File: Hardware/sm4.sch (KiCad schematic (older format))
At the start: 91 parts, among them J1 Motor1, J2 Termination, J3 CAN bus, J4 Motor2, J5 I2C, J6 Power, J7 USB_C_Receptacle_USB2.0, J8 Conn_01x05_Male, Q1 NDT2955, SW1 RST_SW, SW2 BOOT_SW, U1 STM32F412RETx, U2 TMC2100-TA, U3 MCP2562-E-SN, U4 TMC2100-TA, U6 MCP1700-3302E_SOT23, U7 USBLC6-2SC6, Y1 25 MHz

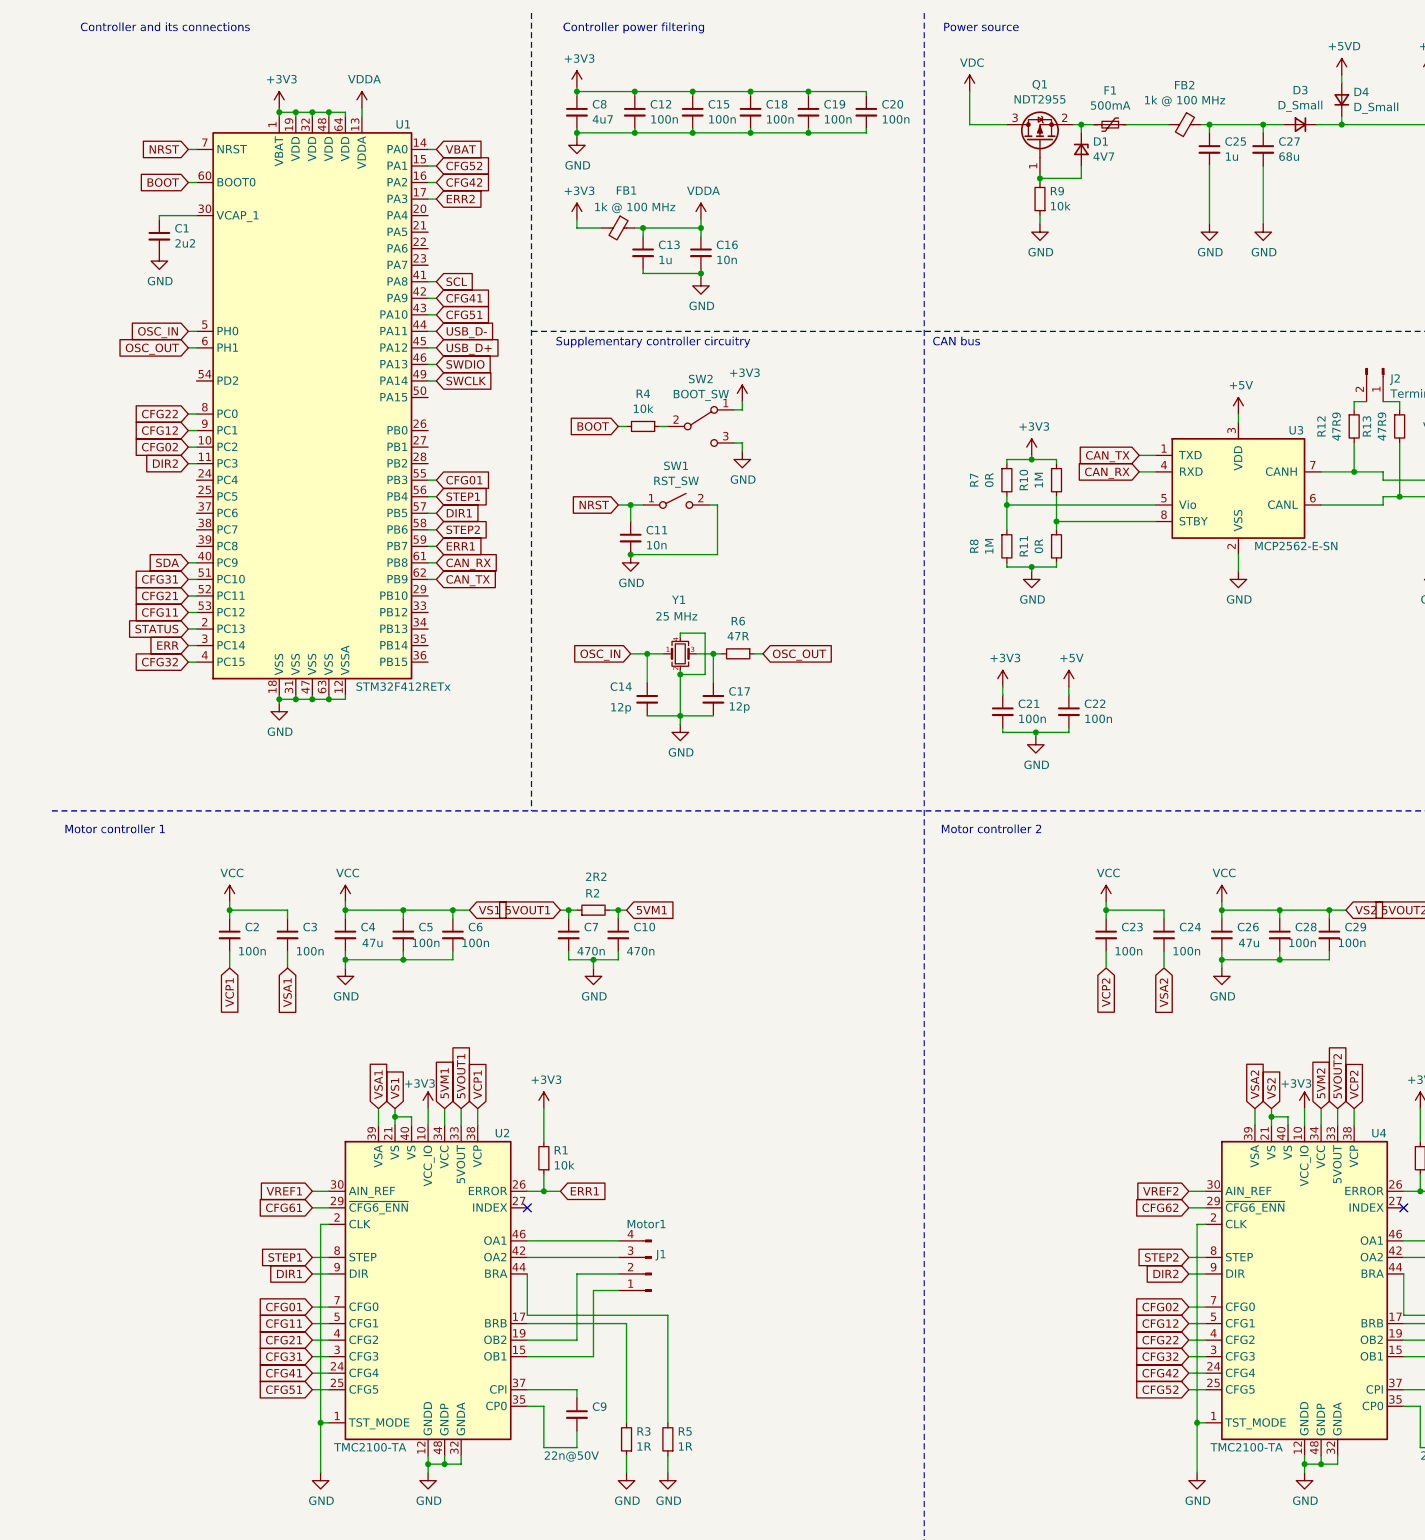
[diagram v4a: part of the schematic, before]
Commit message: Implement more of the second version of the PCB.
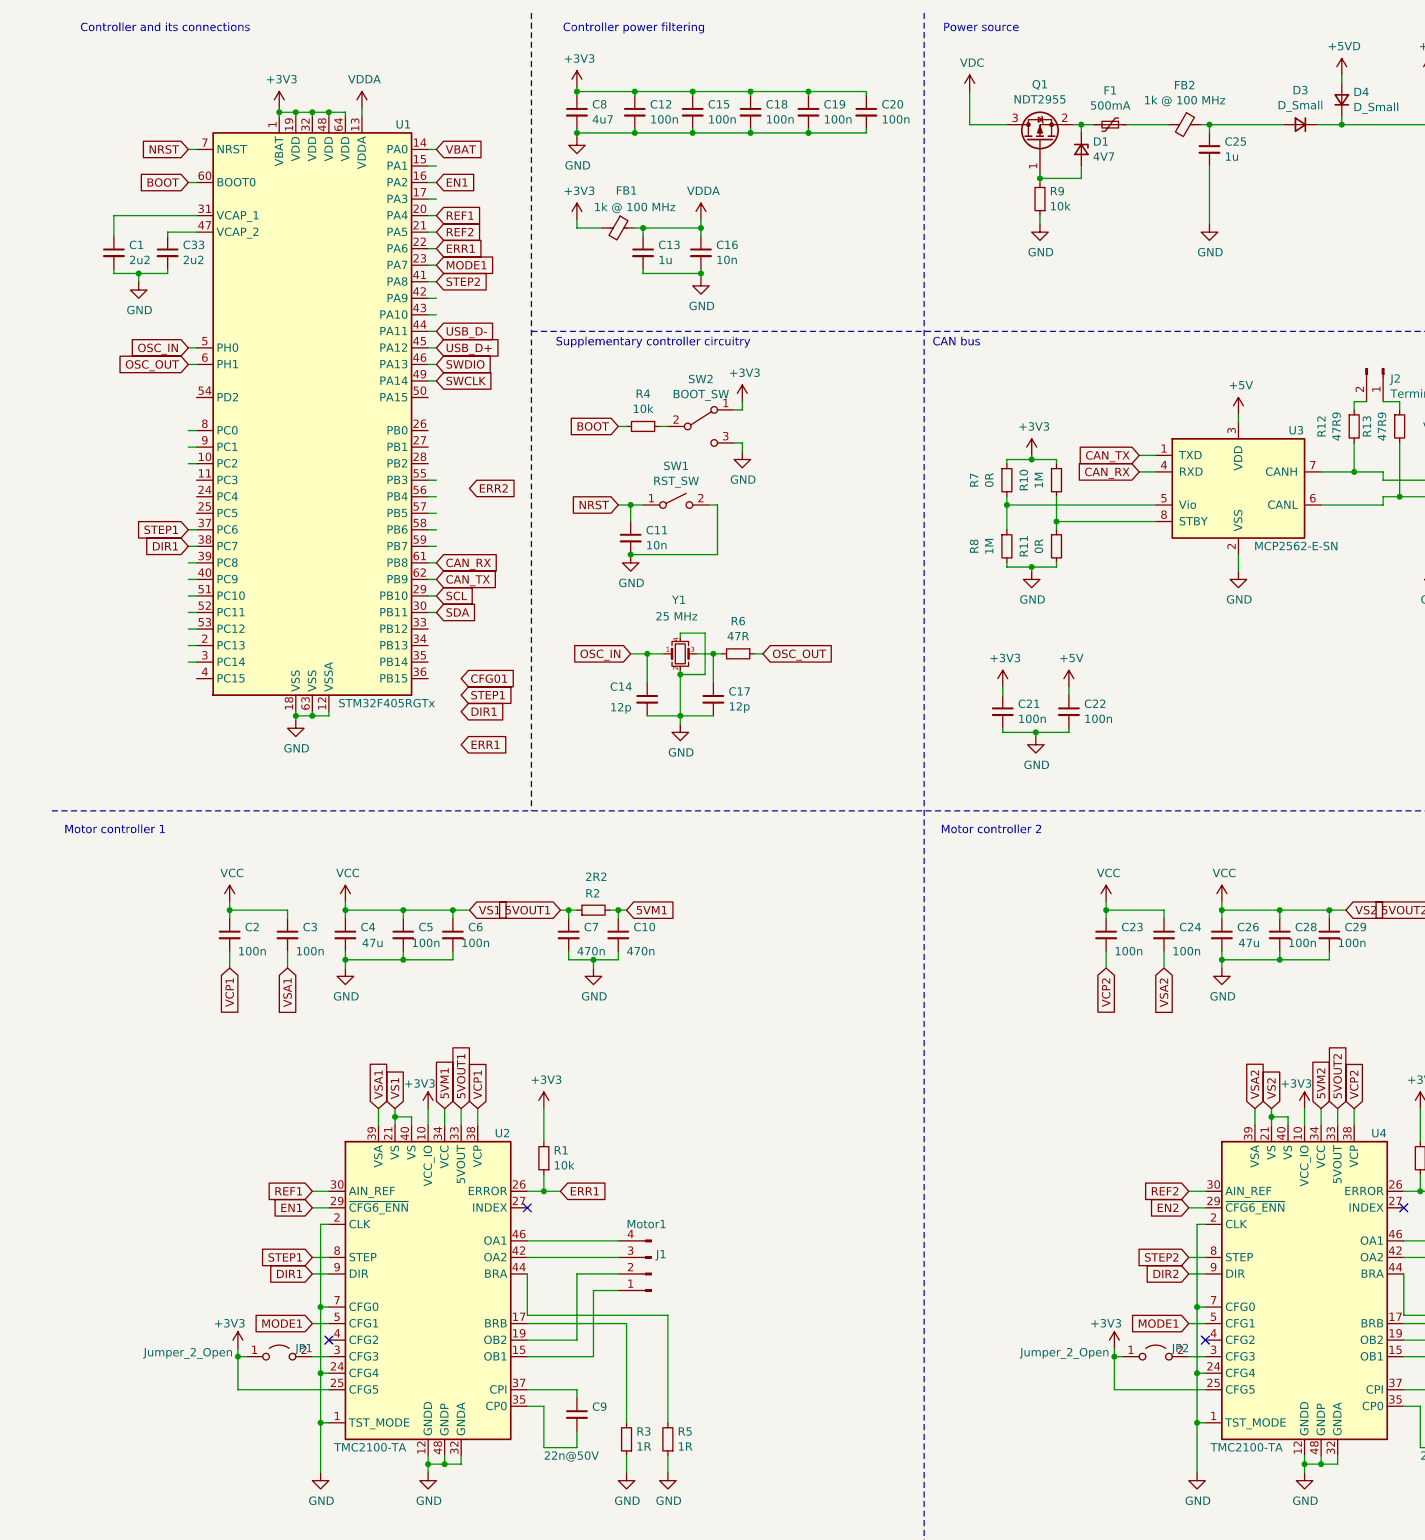
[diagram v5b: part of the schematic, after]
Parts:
- removed C27: 68u, Capacitor_SMD:C_Elec_6.3x7.7, symbol Device:C_Small
- removed U1: STM32F412RETx, Package_QFP:LQFP-64_10x10mm_P0.5mm, symbol MCU_ST_STM32F4:STM32F412RETx
- added C33: 2u2, Capacitor_SMD:C_0603_1608Metric_Pad1.08x0.95mm_HandSolder, symbol Device:C_Small
- added JP1, JP2: Jumper_2_Open, Jumper:SolderJumper-2_P1.3mm_Open_TrianglePad1.0x1.5mm, symbol Jumper:Jumper_2_Open
- added U1: STM32F405RGTx, Package_QFP:LQFP-64_10x10mm_P0.5mm, symbol MCU_ST_STM32F4:STM32F405RGTx
- C12, C14, C15, C16, C17, C18, C19, C20, C21, C22, C36: footprint Capacitor_SMD:C_0603_1608Metric_Pad1.08x0.95mm_HandSolder -> Capacitor_SMD:C_0402_1005Metric_Pad0.74x0.62mm_HandSolder
- R1, R10, R11, R18, R19, R20, R21, R22, R23, R24, R4, R6, R7, R8: footprint Resistor_SMD:R_0603_1608Metric_Pad0.98x0.95mm_HandSolder -> Resistor_SMD:R_0402_1005Metric_Pad0.72x0.64mm_HandSolder
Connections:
- net labels added: EN1, EN2, MODE1, REF1, REF2
- net labels removed: CFG02, CFG11, CFG12, CFG21, CFG22, CFG31, CFG32, CFG41, CFG42, CFG51, CFG52, CFG61, CFG62, VREF1, VREF2
- wire segments 439 -> 454
- no-connect marks 4 -> 6
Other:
- moved on the sheet: C1
